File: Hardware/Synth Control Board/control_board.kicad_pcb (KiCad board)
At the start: 2 copper layers, 157.5 x 154.9 mm, 60 parts, among them J1 Conn_02x13_Odd_Even, J10 Conn_01x05, J11 Conn_01x08, J2 Conn_01x03, J3 Conn_02x13_Odd_Even, J5 Conn_01x08, J7 Conn_01x05, J8 Conn_01x05, J9 Conn_01x05, SW1 SW_DPDT_x2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

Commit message: temporary global feedback control
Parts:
- removed J5: Conn_01x08, Pin_Headers:Pin_Header_Straight_1x08_Pitch2.54mm
- added C1: C_Small, digikey-footprints:0805, F.Cu at (85.8, 26.7)
- added J4: Conn_01x08, Pin_Headers:Pin_Header_Straight_1x10_Pitch2.54mm, F.Cu at (72.4, 115.6)
- added R1: R, digikey-footprints:0805, F.Cu at (85.9, 23.5)
- added RV29: 10kA, Potentiometers:Potentiometer_Bourns_PTV09A-1_Horizontal, F.Cu at (84.9, 20.0)
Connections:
- RV15 pad 3: /freq_fb_2 -> Net-(RV15-Pad3)
- RV15 pad 4: /freq_fb_2 -> Net-(RV15-Pad3)
- RV15 pad 5: /freq_fb_2 -> Net-(RV15-Pad3)
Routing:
- net /delay_in: track 0.00 -> 115.7 mm, vias 0 -> 4
- net /delay_fb_in: track 0.00 -> 52.9 mm
- net /delay_in_1: track 72.0 -> 19.1 mm
- net /delay_out_3: track 43.6 -> 2.09 mm
- net /delay_out: track 0.00 -> 41.5 mm
- net /delay_time_in: track 0.00 -> 34.9 mm
- net /delay_in_2: track 51.9 -> 17.0 mm
- net Net-(RV15-Pad3): track 0.00 -> 11.3 mm
- net /freq_fb_2: track 23.7 -> 12.4 mm
- net Net-(C1-Pad2): track 0.00 -> 8.36 mm
- net /delay_in_3: track 32.3 -> 26.5 mm
- net /delay_out_2: track 60.7 -> 56.3 mm
- net /delay_time_out: track 0.00 -> 4.39 mm
- net Net-(R1-Pad1): track 0.00 -> 3.56 mm
- net /delay_out_1: track 77.4 -> 76.2 mm
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
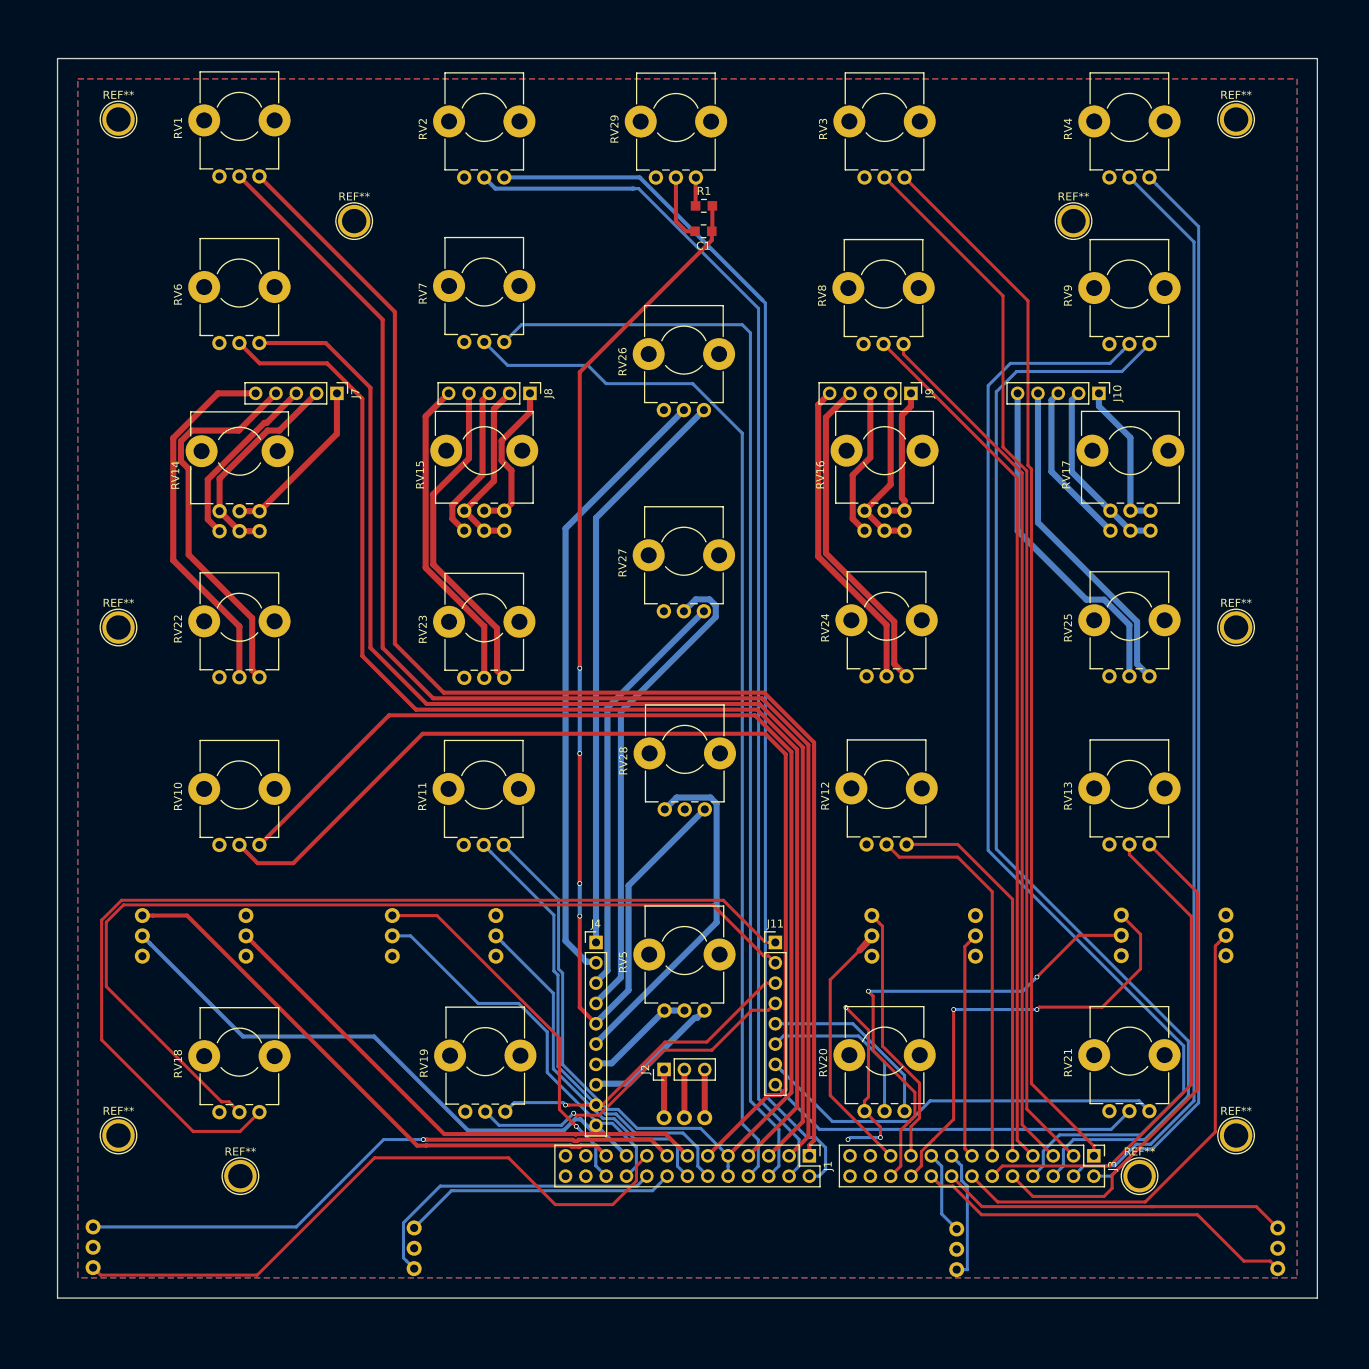
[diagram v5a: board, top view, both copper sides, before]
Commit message: fix filter pots. Dual ganged pot footprint was incorrect.
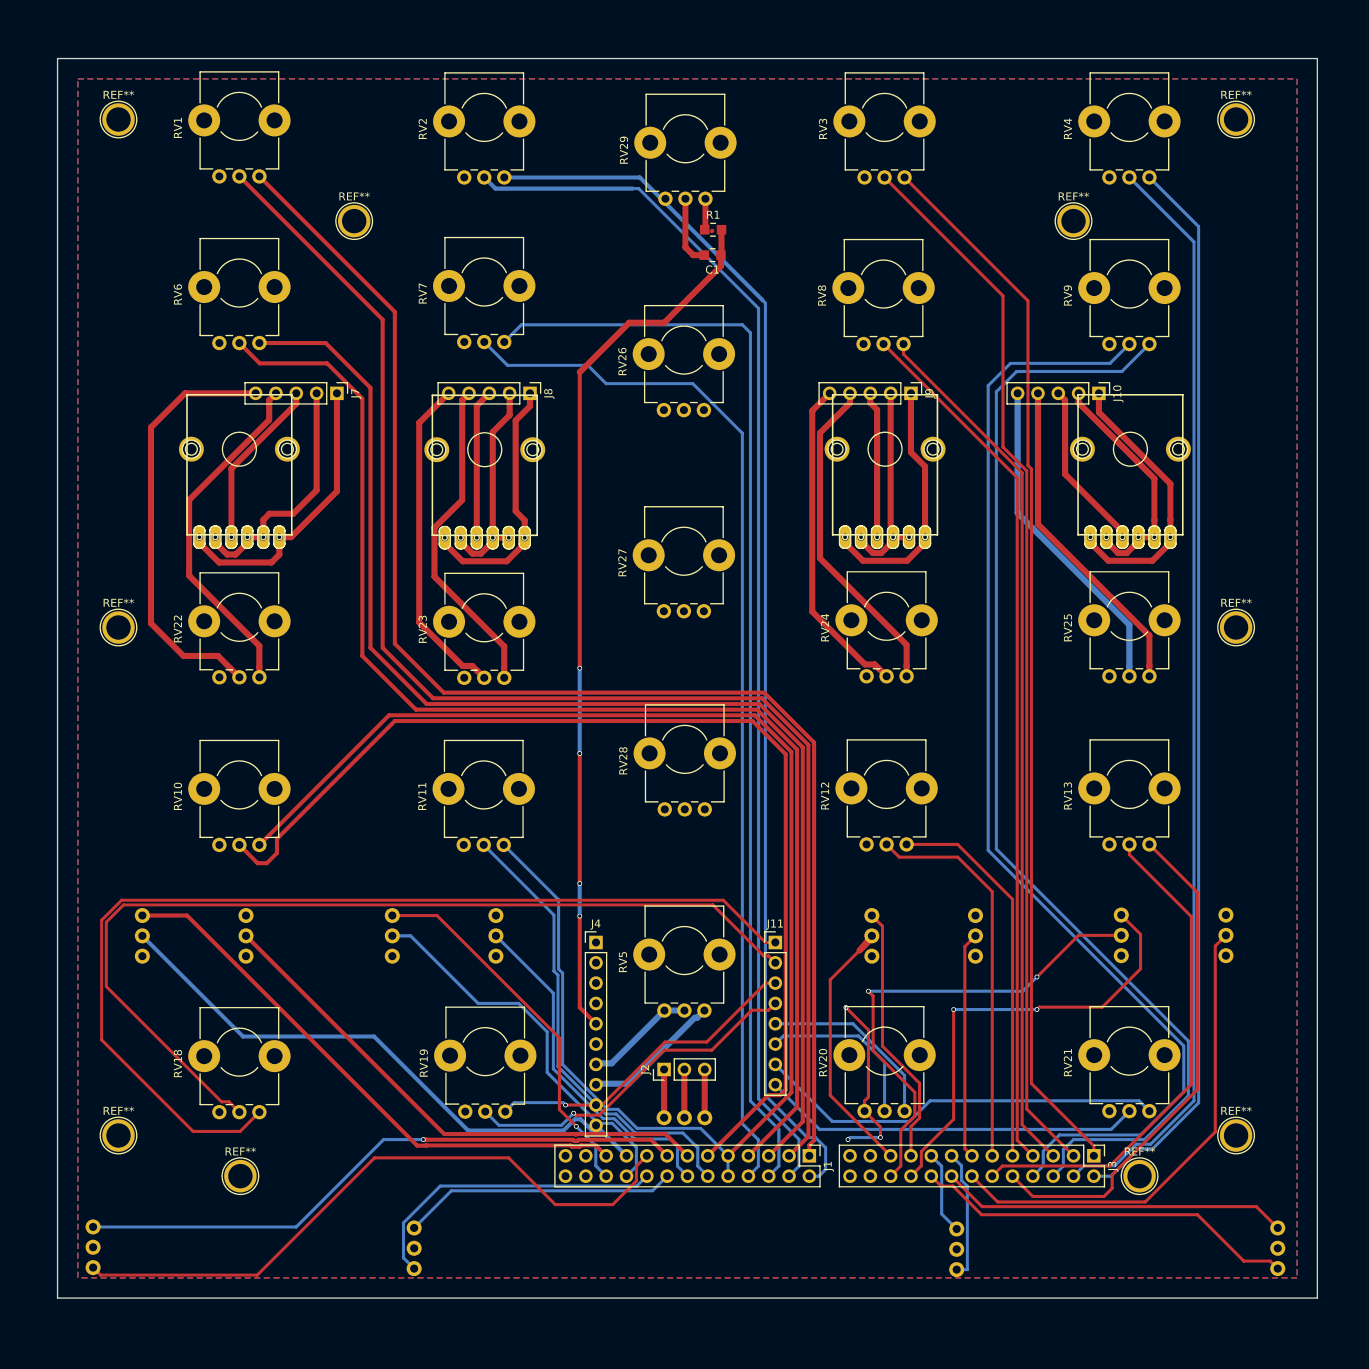
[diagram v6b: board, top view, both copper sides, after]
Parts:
- RV14, RV15, RV16, RV17: value POT_Dual -> POT_DUAL; footprint Potentiometers:Potentiometer_Alps_RK09L_Double_Horizontal -> SparkFun-Electromechanical:POT_PANASONIC_DUAL_VERT_KIT
- moved RV17 114.1 mm to (27.8, 53.9), turned to 270 degrees
- moved RV15 48.2 mm to (108.5, 53.9), turned to 270 degrees
- moved RV16 29.3 mm to (139.2, 53.9), turned to 270 degrees
- moved RV14 29.2 mm to (58.5, 54.0), turned to 270 degrees
- moved R1 3.20 mm to (87.0, 26.5)
- moved C1 3.20 mm to (87.0, 29.7)
- moved RV29 2.91 mm to (86.1, 22.6)
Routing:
- net /delay_out_1: track 76.2 -> 0.00 mm
- net /delay_out_2: track 56.3 -> 0.00 mm
- net /delay_fb_in: track 52.9 -> 0.00 mm
- net /delay_out: track 41.5 -> 0.00 mm
- net /delay_time_in: track 34.9 -> 0.00 mm
- net /delay_in_3: track 26.5 -> 0.00 mm
- net /delay_in_1: track 19.1 -> 0.00 mm
- net /delay_in_2: track 17.0 -> 0.00 mm
- net /freq_in_4: track 18.8 -> 35.0 mm
- net /freq_fb_2: track 12.4 -> 27.8 mm
- net /freq_in_1: track 21.2 -> 36.1 mm
- net /freq_in_3: track 17.8 -> 32.0 mm
- net /freq_in_2: track 19.5 -> 32.5 mm
- net Net-(RV15-Pad3): track 11.3 -> 0.00 mm
- net /lfo_out_1: track 45.9 -> 53.2 mm
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
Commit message: add end stop resistors and reservoir caps to potentiometers.
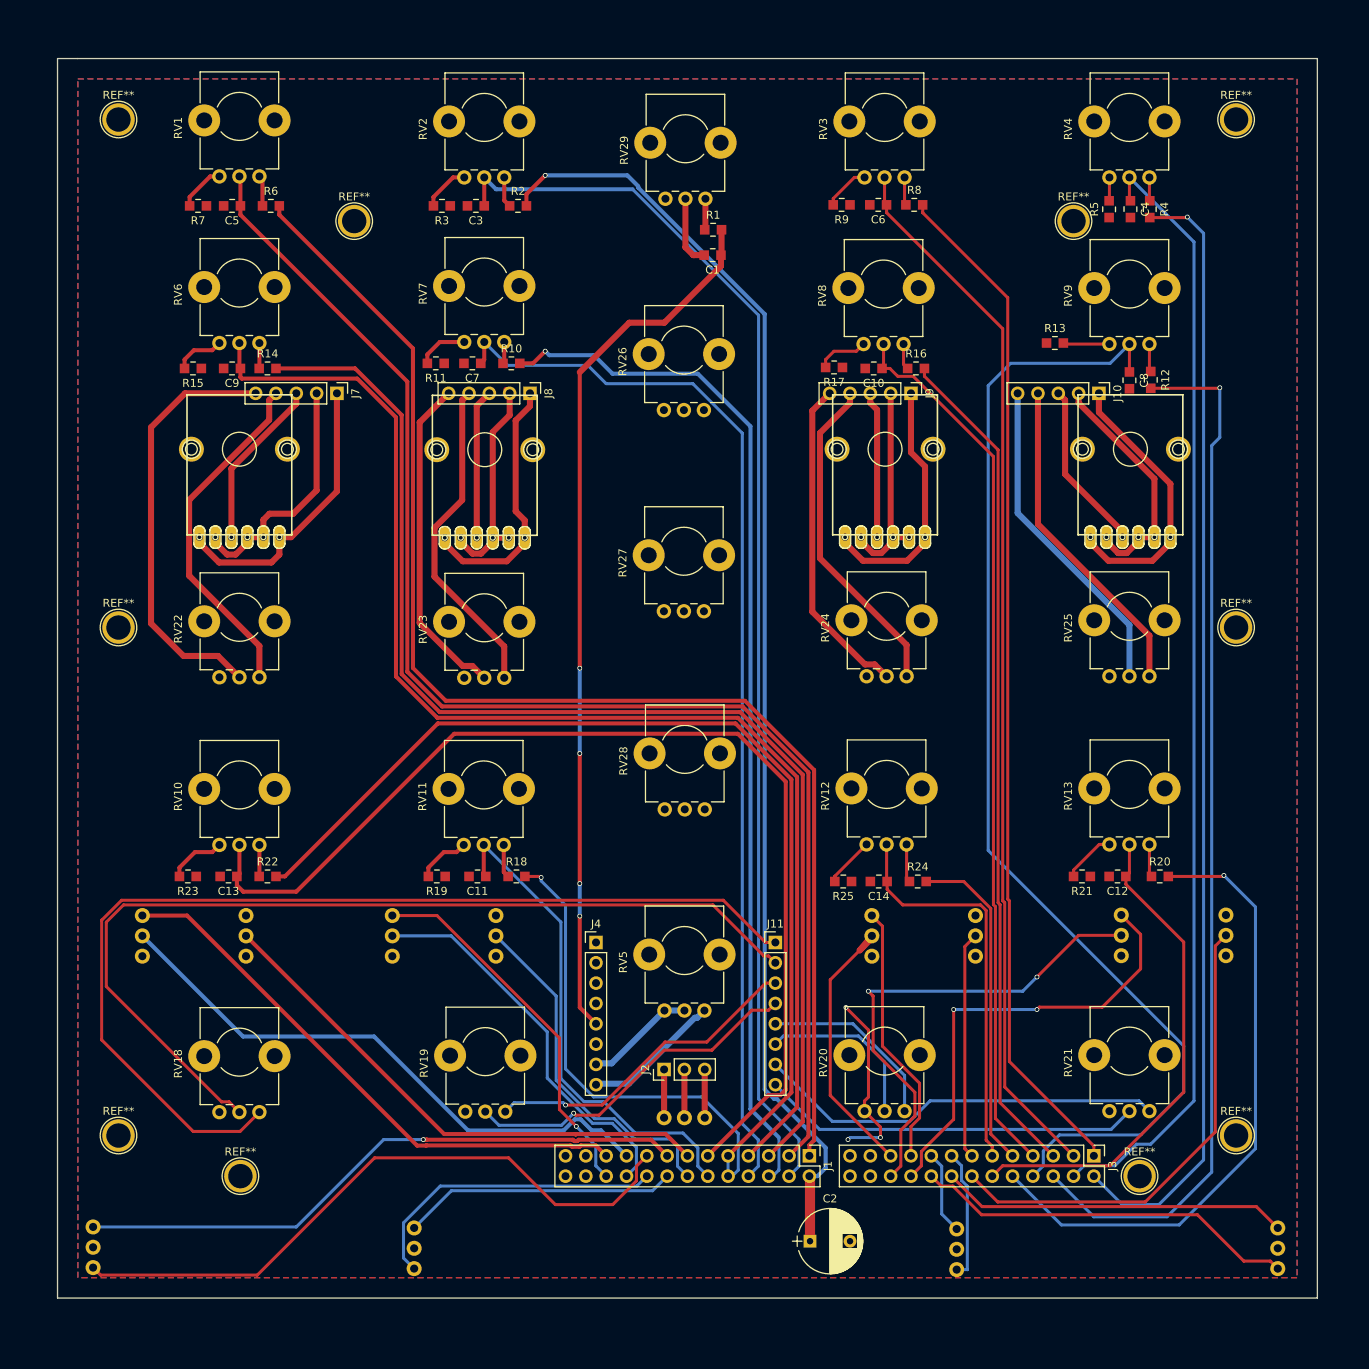
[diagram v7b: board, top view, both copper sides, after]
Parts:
- added C10: C_Small, digikey-footprints:0805, F.Cu at (107.1, 43.8)
- added C11: C_Small, digikey-footprints:0805, F.Cu at (57.6, 107.3)
- added C12: C_Small, digikey-footprints:0805, F.Cu at (137.6, 107.3)
- added C13: C_Small, digikey-footprints:0805, F.Cu at (26.4, 107.3)
- added C14: C_Small, digikey-footprints:0805, F.Cu at (107.7, 108.0)
- added C2: 10uF, Capacitors_THT:CP_Radial_D8.0mm_P5.00mm, F.Cu at (99.1, 152.9)
- added C3: C_Small, digikey-footprints:0805, F.Cu at (57.4, 23.5)
- added C4: C_Small, digikey-footprints:0805, F.Cu at (139.2, 23.9)
- added C5: C_Small, digikey-footprints:0805, F.Cu at (26.9, 23.5)
- added C6: C_Small, digikey-footprints:0805, F.Cu at (107.7, 23.4)
- added C7: C_Small, digikey-footprints:0805, F.Cu at (56.9, 43.2)
- added C8: C_Small, digikey-footprints:0805, F.Cu at (139.1, 45.3)
- added C9: C_Small, digikey-footprints:0805, F.Cu at (26.9, 43.8)
- added R10: R, digikey-footprints:0805, F.Cu at (61.8, 43.2)
- added R11: R, digikey-footprints:0805, F.Cu at (52.4, 43.2)
- added R12: R, digikey-footprints:0805, F.Cu at (141.7, 45.2)
- added R13: R, digikey-footprints:0805, F.Cu at (129.8, 40.6)
- added R14: R, digikey-footprints:0805, F.Cu at (31.3, 43.8)
- added R15: R, digikey-footprints:0805, F.Cu at (22.0, 43.8)
- added R16: R, digikey-footprints:0805, F.Cu at (112.4, 43.8)
- added R17: R, digikey-footprints:0805, F.Cu at (102.1, 43.7)
- added R18: R, digikey-footprints:0805, F.Cu at (62.5, 107.3)
- added R19: R, digikey-footprints:0805, F.Cu at (52.5, 107.3)
- added R2: R, digikey-footprints:0805, F.Cu at (62.6, 23.5)
- added R20: R, digikey-footprints:0805, F.Cu at (142.9, 107.3)
- added R21: R, digikey-footprints:0805, F.Cu at (133.1, 107.3)
- added R22: R, digikey-footprints:0805, F.Cu at (31.3, 107.3)
- added R23: R, digikey-footprints:0805, F.Cu at (21.4, 107.3)
- added R24: R, digikey-footprints:0805, F.Cu at (112.6, 108.0)
- added R25: R, digikey-footprints:0805, F.Cu at (103.3, 108.0)
- added R3: R, digikey-footprints:0805, F.Cu at (53.1, 23.5)
- added R4: R, digikey-footprints:0805, F.Cu at (141.6, 23.9)
- added R5: R, digikey-footprints:0805, F.Cu at (136.5, 23.9)
- added R6: R, digikey-footprints:0805, F.Cu at (31.8, 23.5)
- added R7: R, digikey-footprints:0805, F.Cu at (22.6, 23.5)
- added R8: R, digikey-footprints:0805, F.Cu at (112.2, 23.4)
- added R9: R, digikey-footprints:0805, F.Cu at (103.1, 23.4)
- J4: footprint Pin_Headers:Pin_Header_Straight_1x10_Pitch2.54mm -> Pin_Headers:Pin_Header_Straight_1x08_Pitch2.54mm
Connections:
- RV1 pad 1: +5V -> Net-(R6-Pad1)
- RV1 pad 3: GND -> Net-(R7-Pad2)
- RV10 pad 1: +5V -> Net-(R22-Pad1)
- RV10 pad 3: GND -> Net-(R23-Pad2)
- RV11 pad 1: +5V -> Net-(R18-Pad1)
- RV11 pad 3: GND -> Net-(R19-Pad2)
- RV12 pad 1: +5V -> Net-(R24-Pad1)
- RV12 pad 3: GND -> Net-(R25-Pad2)
- RV13 pad 1: +5V -> Net-(R20-Pad1)
- RV13 pad 3: GND -> Net-(R21-Pad2)
- RV2 pad 1: +5V -> Net-(R2-Pad1)
- RV2 pad 3: GND -> Net-(R3-Pad2)
- RV3 pad 1: +5V -> Net-(R8-Pad1)
- RV3 pad 3: GND -> Net-(R9-Pad2)
- RV4 pad 1: +5V -> Net-(R4-Pad1)
- RV4 pad 3: GND -> Net-(R5-Pad2)
- RV6 pad 1: +5V -> Net-(R14-Pad1)
- RV6 pad 3: GND -> Net-(R15-Pad2)
- RV7 pad 1: +5V -> Net-(R10-Pad1)
- RV7 pad 3: GND -> Net-(R11-Pad2)
- RV8 pad 1: +5V -> Net-(R16-Pad1)
- RV8 pad 3: GND -> Net-(R17-Pad2)
- RV9 pad 1: +5V -> Net-(R12-Pad1)
- RV9 pad 3: GND -> Net-(R13-Pad2)
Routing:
- net +5V: track 1446.2 -> 1426.2 mm, vias 0 -> 6
- net Net-(R23-Pad2): track 0.00 -> 7.27 mm
- net Net-(R19-Pad2): track 0.00 -> 6.70 mm
- net Net-(R21-Pad2): track 0.00 -> 6.60 mm
- net Net-(R17-Pad2): track 0.00 -> 6.52 mm
- net Net-(R11-Pad2): track 0.00 -> 6.37 mm
- net Net-(R15-Pad2): track 0.00 -> 6.32 mm
- net Net-(R25-Pad2): track 0.00 -> 6.28 mm
- net Net-(R3-Pad2): track 0.00 -> 5.97 mm
- net Net-(R7-Pad2): track 0.00 -> 5.90 mm
- net Net-(R13-Pad2): track 0.00 -> 5.81 mm
- net Net-(R9-Pad2): track 0.00 -> 5.80 mm
- net Net-(R24-Pad1): track 0.00 -> 4.78 mm
- net /osc2_speed: track 57.3 -> 62.0 mm
- net Net-(R18-Pad1): track 0.00 -> 4.16 mm
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
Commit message: fix toggle switch footprints
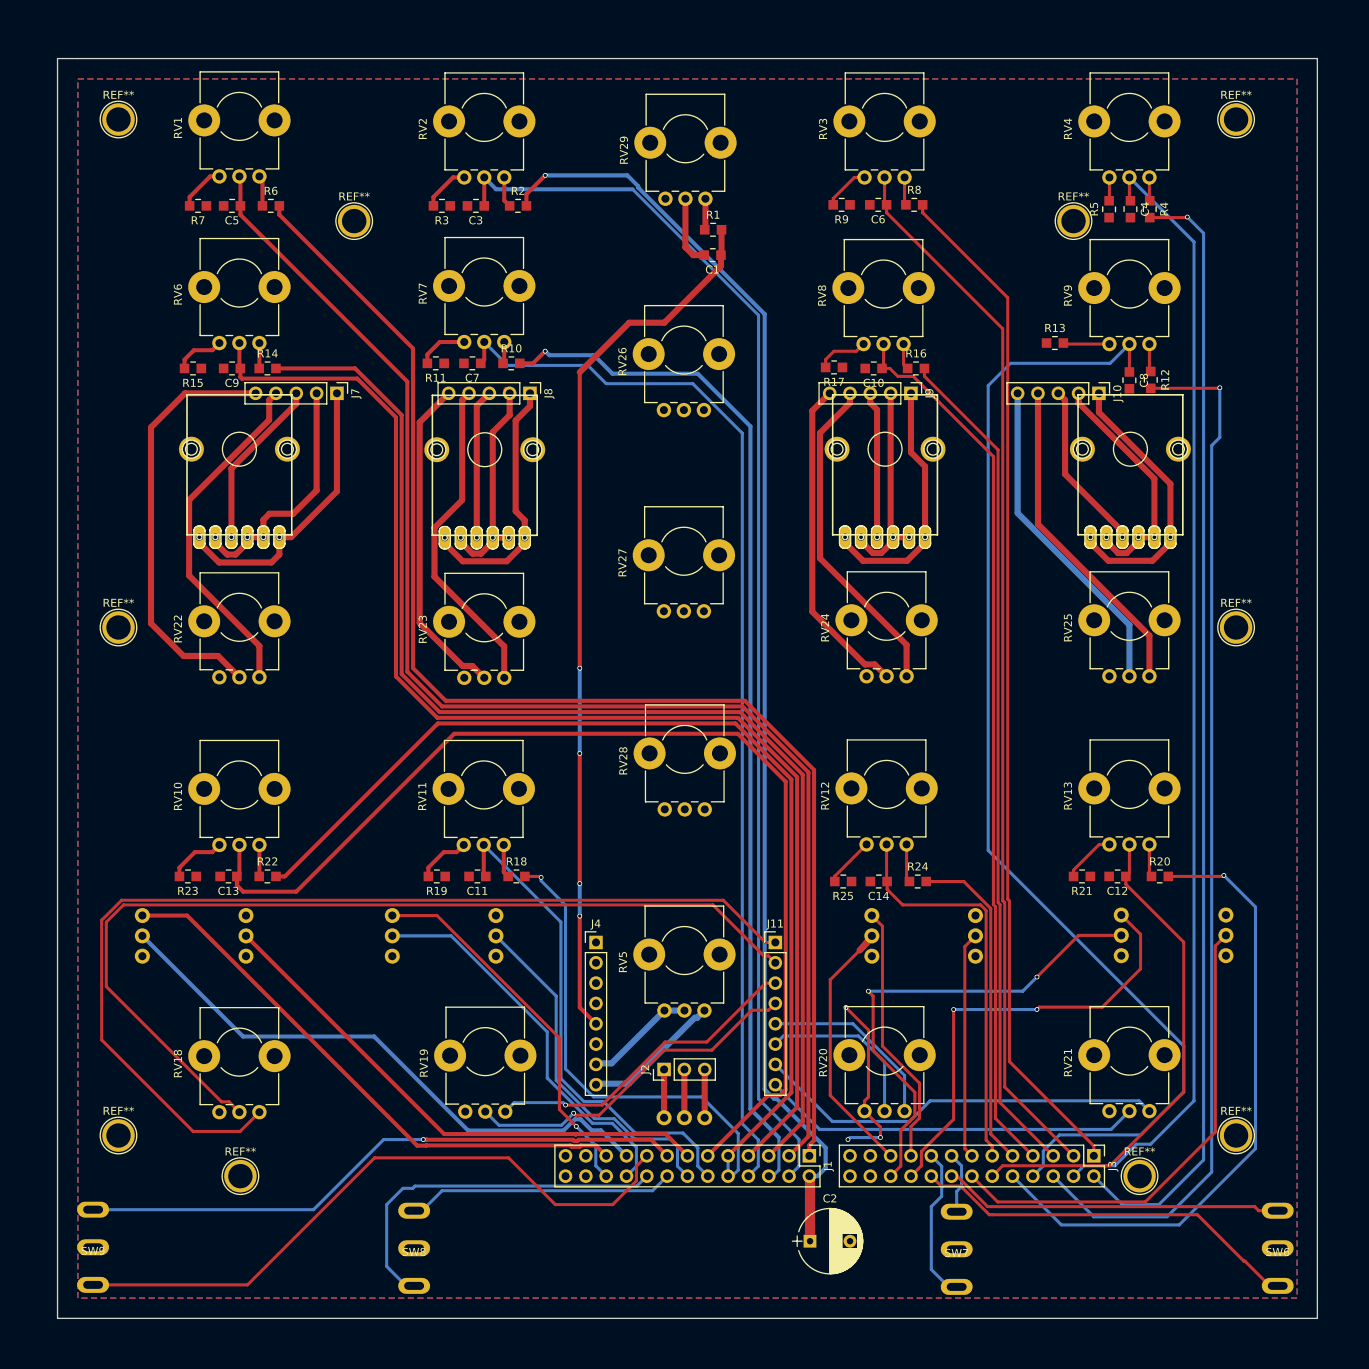
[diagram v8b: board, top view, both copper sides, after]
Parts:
- SW6, SW7, SW8, SW9: footprint SparkFun-Electromechanical:SWITCH-SPDT -> switches:switch_toggle_4.7mm_pitch
- turned SW7 to 0 degrees
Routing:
- net /osc3_repeat: track 10.5 -> 19.4 mm
- net /osc3_hold: track 16.4 -> 7.77 mm
- net /osc2_repeat: track 39.1 -> 46.2 mm
- net /osc4_repeat: track 48.1 -> 49.0 mm
- net /osc4_hold: track 43.4 -> 42.6 mm
- net /osc2_hold: track 34.3 -> 33.4 mm
- net /osc1_hold: track 77.3 -> 76.4 mm
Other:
- board size 157.5 x 154.9 mm -> 157.5 x 157.5 mm
